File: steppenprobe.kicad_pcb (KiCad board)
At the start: 2 copper layers, 50 x 60 mm, 88 parts, among them J1 USB_C_Receptacle_USB2.0, J2 Conn_ST_STDC14, J4 Conn_01x16, Q1 2N7002, SW1 SW_SPDT, SW2 SW_Push, U1 FT2232HL, U10 74LVC1G125, U11 74LVC1G125, U12 74LVC1G125, U2 XC6206PxxxMR, U3 SRV05-4, U4 93LCxxB, U5 74LVC1G125, U6 74LVC1G126, U7 74LVC1G125, U8 74LVC1G125, U9 74LVC1G125, Y1 Crystal_GND24

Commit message: Fixed errors, assigned footprints.
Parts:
- added D7: LED, LED_SMD:LED_0603_1608Metric, F.Cu at (170.2, 89.8)
- added D8: LED, LED_SMD:LED_0603_1608Metric, F.Cu at (170.2, 92.4)
- added J2: Conn_01x12, Connector_PinHeader_2.54mm:PinHeader_1x12_P2.54mm_Vertical, F.Cu at (154.0, 65.1)
- added PMOD1: PMOD-Device-x2-Type-1A-GPIO, pmod-conn_6x2:pmod_pin_array_6x2, F.Cu at (171.4, 71.1)
- added R3: 1k, Resistor_SMD:R_0603_1608Metric, F.Cu at (170.2, 95.0)
- added R5: 1k, Resistor_SMD:R_1206_3216Metric, F.Cu at (170.2, 98.0)
- added TP3: TestPoint, TestPoint:TestPoint_Pad_D1.0mm, F.Cu at (169.7, 80.9)
- added TP4: TestPoint, TestPoint:TestPoint_Pad_D1.0mm, F.Cu at (169.7, 84.0)
- added TP5: TestPoint, TestPoint:TestPoint_Pad_D1.0mm, F.Cu at (169.7, 87.0)
- U2: footprint Package_TO_SOT_SMD:SOT-23 -> Package_TO_SOT_SMD:SOT-23-3
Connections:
- J1 pad A8: unconnected-(J1-PadA8) -> (no net)
- J1 pad B8: unconnected-(J1-PadB8) -> (no net)
- R14 pad 1: /TMS_TRGT -> /TDI_TRGT
- R14 pad 2: /TMS_R -> /TDI_R
- R16 pad 1: /TDI_TRGT -> /TMS_TRGT
- R16 pad 2: /TDI_R -> /TMS_R
- U1 pad 22: /SWD_EN -> unconnected-(U1-ADBUS5-Pad22)
- U1 pad 23: /SWDIO_OE_N -> unconnected-(U1-ADBUS6-Pad23)
- U1 pad 24: /SRST -> unconnected-(U1-ADBUS7-Pad24)
- U1 pad 32: /GPIO_C -> /USR_LED_1
- U1 pad 33: /GPIO_D -> /USR_LED_2
- U1 pad 43: unconnected-(U1-Pad43) -> /DTR_N
- U1 pad 44: unconnected-(U1-Pad44) -> /DSR_N
- U1 pad 45: unconnected-(U1-Pad45) -> /DCD_N
- U1 pad 61: /EE_DATA -> unconnected-(U1-EEDATA-Pad61)
- U1 pad 62: /EE_CLK -> unconnected-(U1-EECLK-Pad62)
- U1 pad 63: /EE_CS -> unconnected-(U1-EECS-Pad63)
- U11 pad 2: /RXD_IN -> /RXD_R
- U5 pad 1: /SWD_EN -> GND
- U8 pad 1: /SWD_EN -> GND
- U9 pad 1: /SWD_EN -> GND
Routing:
- net GND: vias 41 -> 46
- net /SWD_EN: vias 5 -> 0
- net /RXD_R: vias 0 -> 4
- net /RXD_IN: vias 4 -> 0

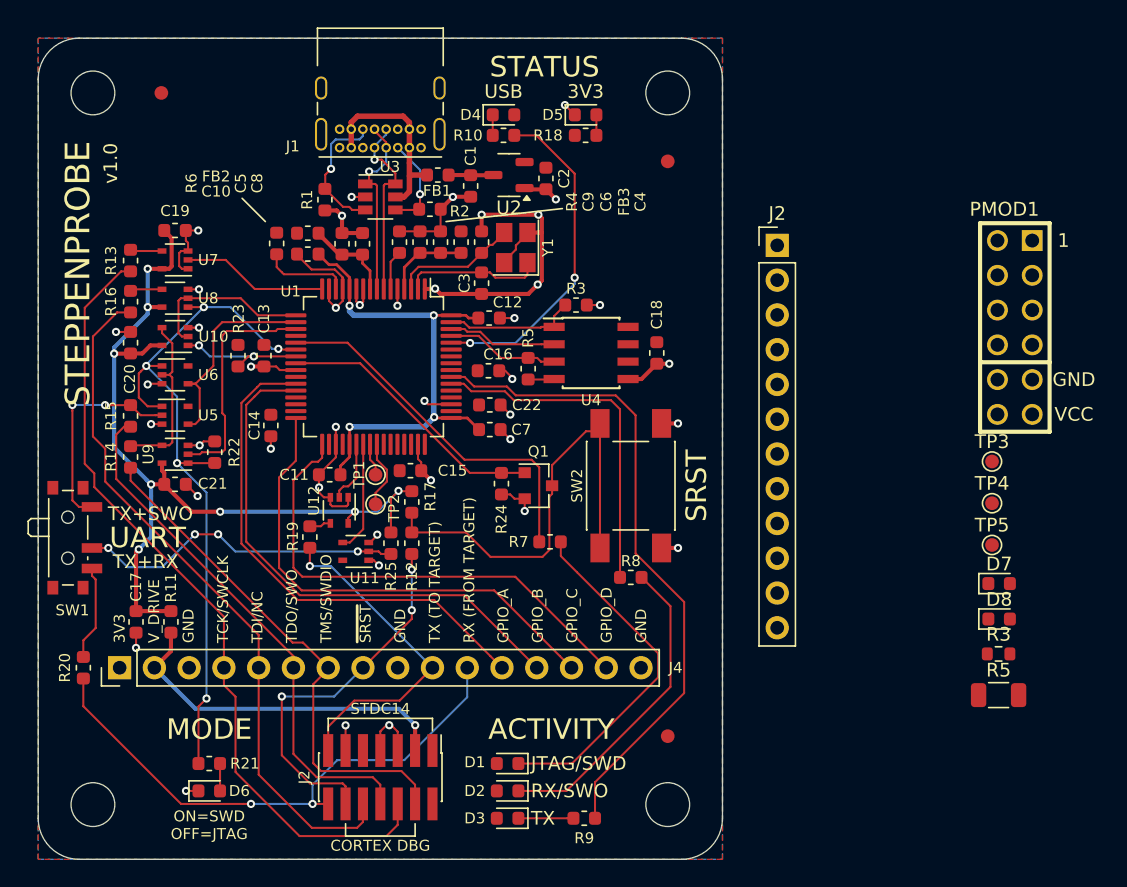
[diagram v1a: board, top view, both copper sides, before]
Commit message: Updated footprints, removed testpoints, edited PCB layout.
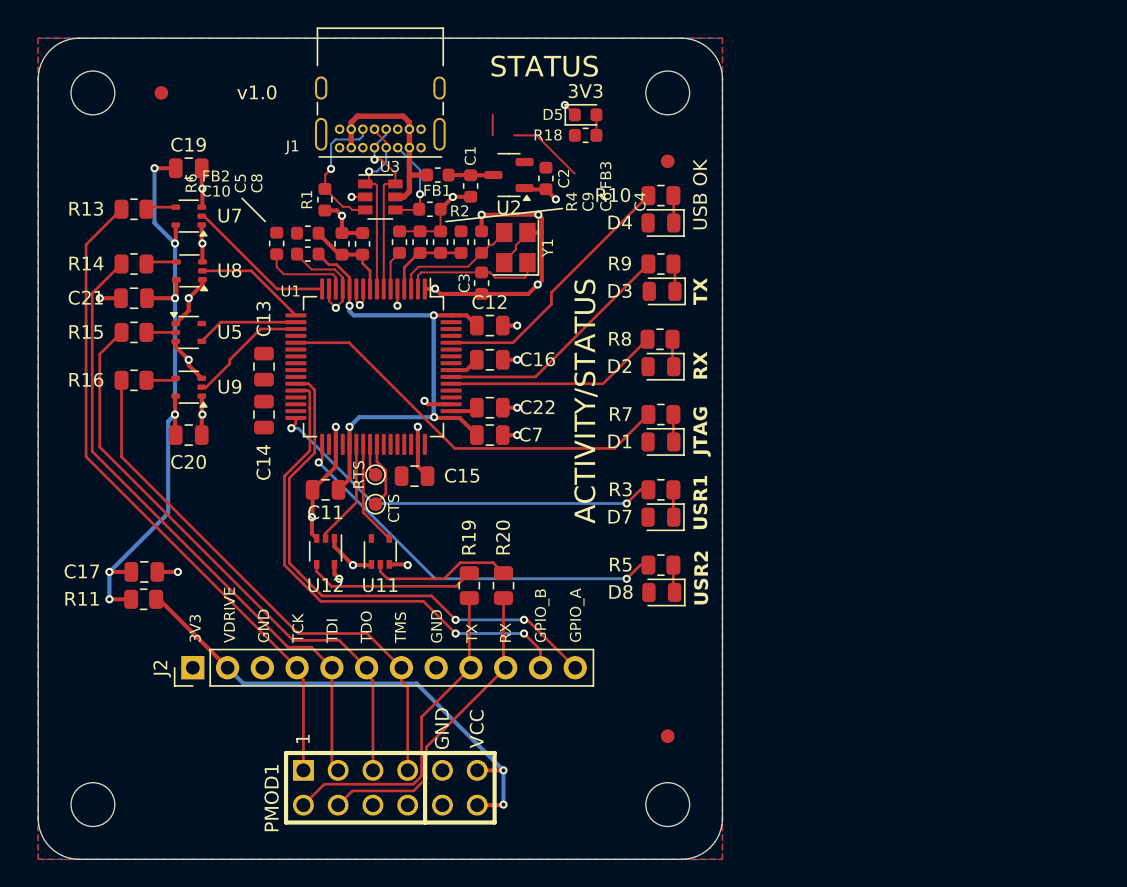
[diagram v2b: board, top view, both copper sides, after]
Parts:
- removed C18: 100nF, Capacitor_SMD:C_0603_1608Metric
- removed D6: LED, LED_SMD:LED_0603_1608Metric
- removed the J2 at (125.0, 104.0)
- removed J4: Conn_01x16, Connector_PinHeader_2.54mm:PinHeader_1x16_P2.54mm_Vertical
- removed Q1: 2N7002, Package_TO_SOT_SMD:SOT-23
- removed R12: 100R, Resistor_SMD:R_0603_1608Metric
- removed R17, R22, R23, R24: 10k, Resistor_SMD:R_0603_1608Metric
- removed R21: 1k, Resistor_SMD:R_0603_1608Metric
- removed R25: 100k, Resistor_SMD:R_0603_1608Metric
- removed the R3 at (139.3, 69.5)
- removed the R5 at (135.8, 74.2)
- removed SW1: SW_SPDT, Button_Switch_SMD:SW_SPDT_PCM12
- removed SW2: SW_Push, Button_Switch_SMD:SW_Push_1P1T_NO_E-Switch_TL3301NxxxxxG
- removed TP3, TP4, TP5: TestPoint, TestPoint:TestPoint_Pad_D1.0mm
- removed U10: 74LVC1G125, Package_TO_SOT_SMD:SOT-353_SC-70-5
- removed U4: 93LCxxB, Package_SO:SOIC-8_3.9x4.9mm_P1.27mm
- removed U6: 74LVC1G126, Package_TO_SOT_SMD:SOT-353_SC-70-5
- C11, C12, C13, C14, C15, C16, C17, C19, C20, C21, C22, C7: footprint Capacitor_SMD:C_0603_1608Metric -> Capacitor_SMD:C_0805_2012Metric
- D1, D2, D3, D4, D7, D8: footprint LED_SMD:LED_0603_1608Metric -> LED_SMD:LED_0805_2012Metric
- R10, R11, R13, R14, R15, R16, R19, R20, R3, R7, R8, R9: footprint Resistor_SMD:R_0603_1608Metric -> Resistor_SMD:R_0805_2012Metric
- R5: footprint Resistor_SMD:R_1206_3216Metric -> Resistor_SMD:R_0805_2012Metric
- moved PMOD1 56.7 mm to (125.7, 104.8), turned to 90 degrees
- moved J2 52.7 mm to (111.3, 96.0), turned to 90 degrees
- moved R9 40.9 mm to (145.5, 66.5), turned to 180 degrees
- moved D3 40.1 mm to (145.6, 68.5)
- moved D2 33.0 mm to (145.5, 74.0)
- moved R20 31.3 mm to (134.0, 90.0)
- moved R3 27.4 mm to (145.5, 83.0)
- moved R5 26.4 mm to (145.5, 88.5)
- moved D1 26.0 mm to (145.5, 79.5)
- moved D7 25.2 mm to (145.5, 85.0), turned to 180 degrees
- moved D8 24.7 mm to (145.6, 90.5), turned to 180 degrees
- moved R8 17.5 mm to (145.4, 72.0)
- moved R14 14.1 mm to (107.0, 66.5), turned to 0 degrees
- moved D4 14.0 mm to (145.5, 63.5), turned to 180 degrees
- moved C21 13.9 mm to (107.0, 69.0), turned to 180 degrees
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- renumbered TP2 to CTS, TP1 to RTS
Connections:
- J2 pad 11: /GPIO_A -> /GPIO_B
- J2 pad 12: /GPIO_B -> /GPIO_A
- U1 pad 43: /DTR_N -> unconnected-(U1-BDBUS4-Pad43)
- U1 pad 44: /DSR_N -> unconnected-(U1-BDBUS5-Pad44)
- U1 pad 45: /DCD_N -> unconnected-(U1-BDBUS6-Pad45)
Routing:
- net /SWD_EN: track 54.7 -> 0.00 mm
- net /GPIO_D: track 36.0 -> 0.00 mm
- net /GPIO_C: track 35.8 -> 0.00 mm
- net /SRST_N_R: track 31.2 -> 0.00 mm
- net /TX_LED_N: track 48.3 -> 17.8 mm
- net /USR_LED_1: track 0.00 -> 29.7 mm, vias 0 -> 2
- net /USR_LED_2: track 0.00 -> 29.5 mm, vias 0 -> 2
- net /SRST_N_TRGT: track 27.8 -> 0.00 mm, vias 3 -> 0
- net /RXD_IN: track 24.0 -> 0.00 mm
- net /ACT_LED_K: track 25.7 -> 2.01 mm
- net /RX_LED_K: track 23.1 -> 2.04 mm
- net /SRST: track 20.0 -> 0.00 mm
- net Vdrive: track 66.3 -> 47.7 mm, vias 8 -> 7
- net /RXD_TRGT: track 40.4 -> 22.9 mm, vias 2 -> 0
- net /TDO_R: track 15.5 -> 2.14 mm, vias 2 -> 0
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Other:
- board text added: "ACTIVITY/STATUS"
- board text added: "JTAG"
- board text added: "TCK"
- board text added: "TDI"
- board text added: "TDO"
- board text added: "TMS"
- board text added: "USB OK"
- board text added: "USR1"
- board text added: "USR2"
- board text added: "VDRIVE"
- board text removed: "ACTIVITY"
- board text removed: "CORTEX DBG"
- board text removed: "JTAG/SWD"
- board text removed: "MODE"
- board text removed: "ON=SWD OFF=JTAG"
- board text removed: "RX (FROM TARGET)"
- board text removed: "RX/SWO"
- board text removed: "SRST"
- board text removed: "STDC14"
- board text removed: "STEPPENPROBE"
- board text removed: "TX (TO TARGET)"
- board text removed: "TX+RX"
- board text removed: "TX+SWO"
- board text removed: "UART"
- board text removed: "USB"

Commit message: Updated pcb.
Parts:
- C1, C10, C2, C3, C4, C5, C6, C8, C9: footprint Capacitor_SMD:C_0603_1608Metric -> Capacitor_SMD:C_0805_2012Metric
- D5: footprint LED_SMD:LED_0603_1608Metric -> LED_SMD:LED_0805_2012Metric
- FB1, FB2, FB3: footprint Inductor_SMD:L_0603_1608Metric -> Inductor_SMD:L_0805_2012Metric
- R1, R18, R2, R4, R6: footprint Resistor_SMD:R_0603_1608Metric -> Resistor_SMD:R_0805_2012Metric
- moved D5 40.8 mm to (145.5, 96.0)
- moved R18 37.3 mm to (145.5, 94.0)
- moved R1 5.17 mm to (118.5, 57.2), turned to 90 degrees
- moved C5 4.69 mm to (118.2, 62.5)
- moved C2 4.66 mm to (141.8, 60.0)
- moved C3 4.36 mm to (136.8, 68.2), turned to 0 degrees
- moved C8 4.28 mm to (120.2, 62.5)
- moved U2 4.10 mm to (138.5, 60.0)
- moved FB2 3.87 mm to (116.2, 62.5), turned to 90 degrees
- moved C1 3.74 mm to (135.2, 60.0)
- moved R4 3.42 mm to (123.0, 64.5), turned to 180 degrees
- moved R6 2.49 mm to (118.5, 67.2), turned to 180 degrees
- moved Y1 1.87 mm to (136.8, 65.0)
- moved R2 1.79 mm to (130.2, 61.8)
- moved C4 1.60 mm to (134.0, 64.9)
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- renumbered RTS to TP1, CTS to TP2
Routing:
- net Vdrive: track 47.7 -> 64.8 mm
- net GND: track 94.9 -> 80.6 mm, vias 29 -> 33
- net /VPLL: track 6.62 -> 11.0 mm
- net /USB_LED_N: track 24.9 -> 21.2 mm
- net +5V: track 3.42 -> 6.73 mm
- net /RESET_N: track 6.42 -> 3.24 mm
- net /USB_CC2: track 10.1 -> 13.2 mm
- net /OSCI: track 10.2 -> 12.3 mm
- net /OSCO: track 9.17 -> 11.1 mm
- net /USB_LED_K: track 3.51 -> 2.01 mm
- net /TCK: track 11.1 -> 12.4 mm
- net +1V8: track 37.7 -> 38.9 mm
- net /VPHY: track 6.17 -> 7.34 mm
- net VBUS: track 14.0 -> 15.0 mm
- net /USB_CC1: track 7.15 -> 8.13 mm
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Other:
- board text added: "USB_OK"
- board text added: "vesp-jtag"
- board text removed: "STATUS"
- board text removed: "USB OK"

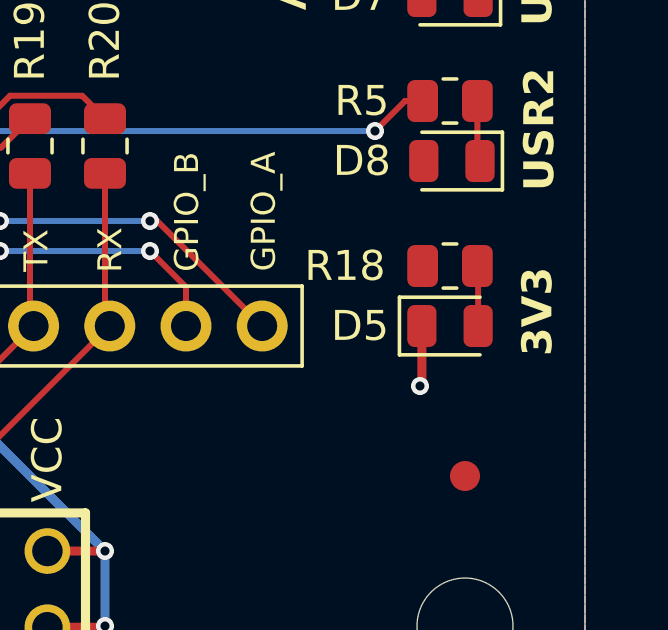
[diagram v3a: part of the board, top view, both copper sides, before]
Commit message: Rotated 3V3 LED.
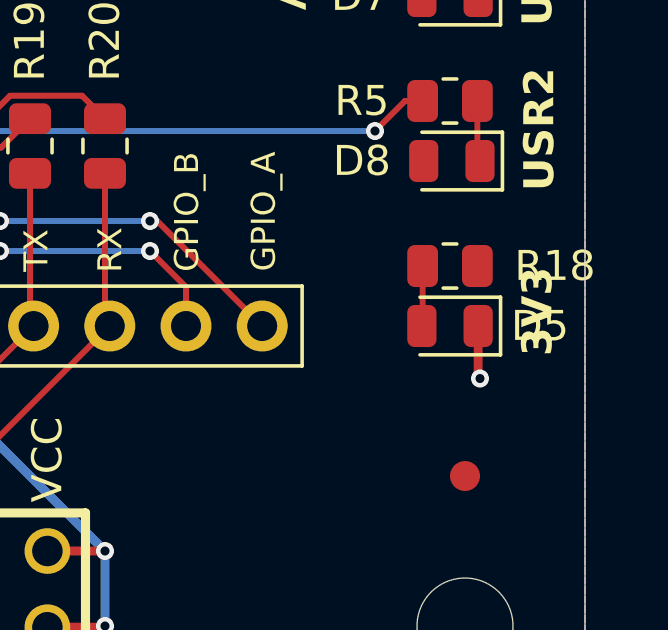
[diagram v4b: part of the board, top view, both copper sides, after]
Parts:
- turned D5 to 180 degrees
- turned R18 to 180 degrees

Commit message: Synced footprints.
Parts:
- moved R19 0.09 mm to (131.5, 90.1)
- moved D8 0.06 mm to (145.5, 90.5)
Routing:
- net /REF: track 3.46 -> 5.67 mm

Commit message: Fixed part numbering.
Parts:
- renumbered C9 to C10, C10 to C11, C13 to C12, C11 to C13, C12 to C15, C15 to C16, C16 to C17, C19 to C18, C20 to C19, C21 to C20, C17 to C21, C22 to C4, C4 to C5, C5 to C6, C6 to C7, C7 to C8, C8 to C9, D5 to D1, D7 to D2, D8 to D3, D2 to D4, D3 to D5, D4 to D6, D1 to D7, R5 to R10, R7 to R11, R13 to R12, R14 to R13, R15 to R14, R16 to R15, R19 to R16, R20 to R17, R11 to R18, R18 to R3, R6 to R5, R8 to R6, R9 to R7, R10 to R8, R3 to R9, U3 to U1, U1 to U3, U5 to U4, U11 to U5, U8 to U6, U9 to U7, U12 to U8, U7 to U9

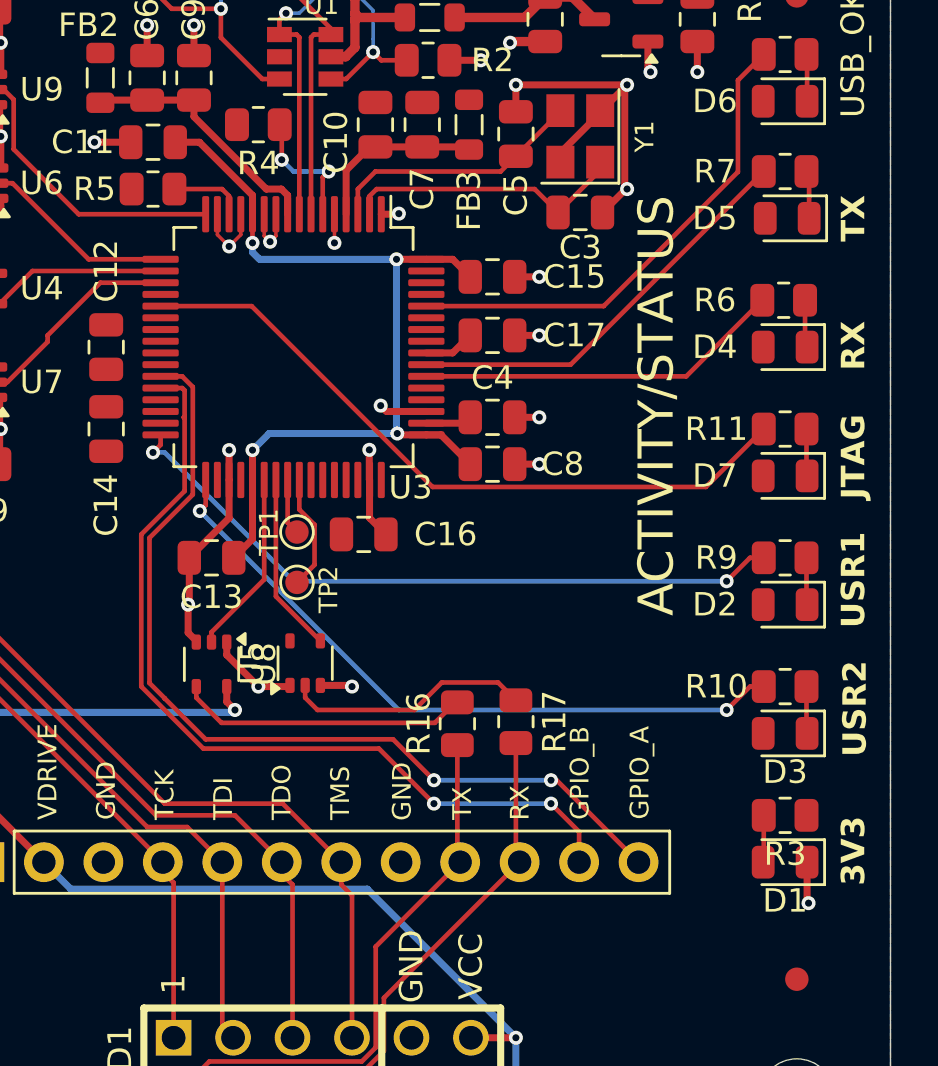
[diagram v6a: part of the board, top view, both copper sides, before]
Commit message: Edited silkscreen graphics.
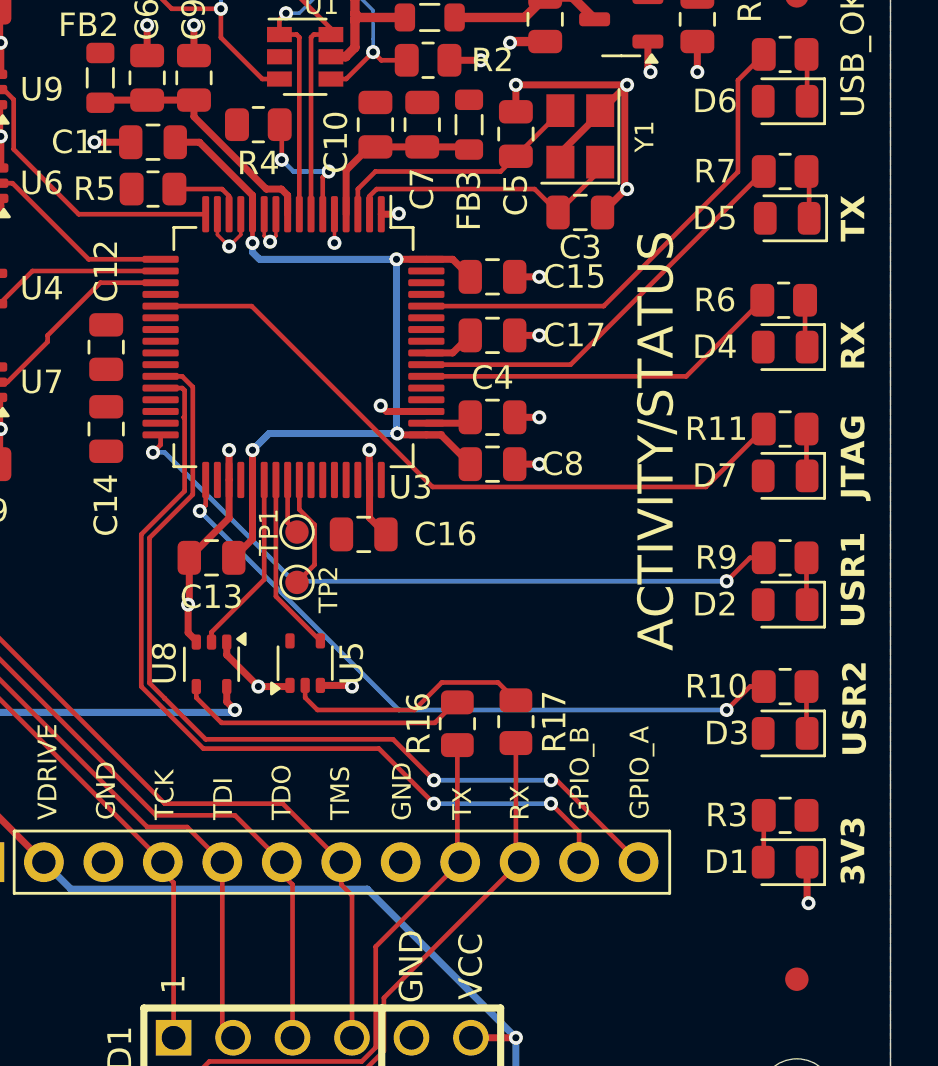
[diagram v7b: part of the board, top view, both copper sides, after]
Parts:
- removed QR*****: qr_steppenprobe_neg, Symbol:qr_steppenprobe_neg
- added G***: LOGO, graphics:vesp-jtag, B.Cu at (124.5, 63.0)
- moved REF** 28.7 mm to (118.5, 75.0)
- moved LOGO1 28.2 mm to (134.0, 75.0)
- moved REF** 9.92 mm to (105.0, 96.5)
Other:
- board text added: "FTDI chip: CHANNEL A = JTAG/GPIOs/USR LEDs CHANNEL B = UART"
- board text added: "github.com/HoneyGol-Microsystems/vesp-jtag"
- board text removed: "(FROM TARGET)"
- board text removed: "(MUST BE POWERED ON J2 OR J4)"
- board text removed: "(TO TARGET)"
- board text removed: "FTDI chip: CHANNEL A = JTAG/SWD+GPIOs CHANNEL B = UART"
- board text removed: "GPIO_C"
- board text removed: "GPIO_D"
- board text removed: "TCK/SWCLK"
- board text removed: "TDI/NC"
- board text removed: "TDO/SWO"
- board text removed: "TMS/SWDIO"
- board text removed: "V_DRIVE"
- board text removed: "github.com/diegoherranz/steppenprobe"
- board text removed: "~{SRST}"
